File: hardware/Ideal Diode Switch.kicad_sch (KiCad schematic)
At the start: 0 parts

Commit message: Schematic is now mostly complete. Will review and then move onto the PCB layout
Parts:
- added C66, C67, C68, C69: 100nF/25VW, Capacitor_SMD:C_0603_1608Metric, symbol Device:C
- added J9: Conn_01x12, Connector_Phoenix_MSTB:PhoenixContact_MSTBVA_2,5_12-G-5,08_1x12_P5.08mm_Vertical, symbol Connector_Generic:Conn_01x12
- added Q10, Q11, Q12, Q5, Q6, Q7, Q8, Q9: SIR880BDP, BidirectionalSupply:POWERPAK-SO-8_L6.2-W5.2-P1.27-BL-EP, symbol BidirectionalSupply:SIR880BDP
- added R35, R39, R43, R47: 97.6K/0.1%, Resistor_SMD:R_0603_1608Metric, symbol Device:R
- added R36, R40, R44: 3.1K/0.1%, Resistor_SMD:R_0603_1608Metric, symbol Device:R
- added R37, R41, R45, R49: 2.1K/1%, Resistor_SMD:R_0603_1608Metric, symbol Device:R
- added R38, R42, R46, R50: 10K, Resistor_SMD:R_0603_1608Metric, symbol Device:R
- added R48: 3.1K/1%, Resistor_SMD:R_0603_1608Metric, symbol Device:R
- added U2, U6, U7, U8: LM74810QDRRRQ1, BidirectionalSupply:WSON-12_L3.0-W3.0-P0.50-TL-EP-2, symbol BidirectionalSupply:LM74810QDRRRQ1
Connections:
- new net: J9.6 (Pin_6), Q8.1 (S), Q8.2 (S), Q8.3 (S), U6.9 (OUT)
- new net: Q8.4 (G), U6.8 (HGATE)
- new net: C67.1, Q7.5 (D), Q7.6 (D), Q7.7 (D), Q7.8 (D), Q7.9 (EP), Q8.5 (D), Q8.6 (D), Q8.7 (D), Q8.8 (D), Q8.9 (EP), U6.10 (VS), U6.12 (C)
- new net: R40.2, R41.1, U6.5 (OV)
- new net: C67.2, U6.11 (CAP)
- new net: Q7.4 (G), U6.1 (DGATE)
- new net: R39.1, U6.4 (SW)
- new net: R36.2, R37.1, U2.5 (OV)
- new net: J9.12 (Pin_12), Q10.1 (S), Q10.2 (S), Q10.3 (S), U7.9 (OUT)
- new net: J9.3 (Pin_3), Q6.1 (S), Q6.2 (S), Q6.3 (S), U2.9 (OUT)
- new net: J9.9 (Pin_9), Q12.1 (S), Q12.2 (S), Q12.3 (S), U8.9 (OUT)
- new net: R47.1, U8.4 (SW)
- new net: C66.1, Q5.5 (D), Q5.6 (D), Q5.7 (D), Q5.8 (D), Q5.9 (EP), Q6.5 (D), Q6.6 (D), Q6.7 (D), Q6.8 (D), Q6.9 (EP), U2.10 (VS), U2.12 (C)
- new net: C66.2, U2.11 (CAP)
- new net: Q9.4 (G), U7.1 (DGATE)
- new net: C68.1, Q10.5 (D), Q10.6 (D), Q10.7 (D), Q10.8 (D), Q10.9 (EP), Q9.5 (D), Q9.6 (D), Q9.7 (D), Q9.8 (D), Q9.9 (EP), U7.10 (VS), U7.12 (C)
- new net: C68.2, U7.11 (CAP)
- new net: R43.1, U7.4 (SW)
- new net: R44.2, R45.1, U7.5 (OV)
- new net: Q10.4 (G), U7.8 (HGATE)
- new net: C69.1, Q11.5 (D), Q11.6 (D), Q11.7 (D), Q11.8 (D), Q11.9 (EP), Q12.5 (D), Q12.6 (D), Q12.7 (D), Q12.8 (D), Q12.9 (EP), U8.10 (VS), U8.12 (C)
- new net: C69.2, U8.11 (CAP)
- new net: Q5.4 (G), U2.1 (DGATE)
- new net: R35.1, U2.4 (SW)
- new net: Q6.4 (G), U2.8 (HGATE)
- new net: Q12.4 (G), U8.8 (HGATE)
- new net: R48.2, R49.1, U8.5 (OV)
- new net: Q11.4 (G), U8.1 (DGATE)
- new net GND: J9.1 (Pin_1), J9.10 (Pin_10), J9.4 (Pin_4), J9.7 (Pin_7), R37.2, R38.2, R41.2, R42.2, R45.2, R46.2, R49.2, R50.2, U2.7 (GND), U6.7 (GND), U7.7 (GND), U8.7 (GND)
- new net SW0_EN: R38.1, U2.6 (EN/UVLO)
- new net SW0_PWR: J9.2 (Pin_2), Q5.1 (S), Q5.2 (S), Q5.3 (S), U2.2 (A), U2.3 (VSNS)
- new net SW0_VSENSE: R35.2, R36.1
- new net SW1_EN: R42.1, U6.6 (EN/UVLO)
- new net SW1_PWR: J9.5 (Pin_5), Q7.1 (S), Q7.2 (S), Q7.3 (S), U6.2 (A), U6.3 (VSNS)
- new net SW1_VSENSE: R39.2, R40.1
- new net SW2_EN: R50.1, U8.6 (EN/UVLO)
- new net SW2_PWR: J9.8 (Pin_8), Q11.1 (S), Q11.2 (S), Q11.3 (S), U8.2 (A), U8.3 (VSNS)
- new net SW2_VSENSE: R47.2, R48.1
- new net SW3_EN: R46.1, U7.6 (EN/UVLO)
- new net SW3_PWR: J9.11 (Pin_11), Q9.1 (S), Q9.2 (S), Q9.3 (S), U7.2 (A), U7.3 (VSNS)
- new net SW3_VSENSE: R43.2, R44.1

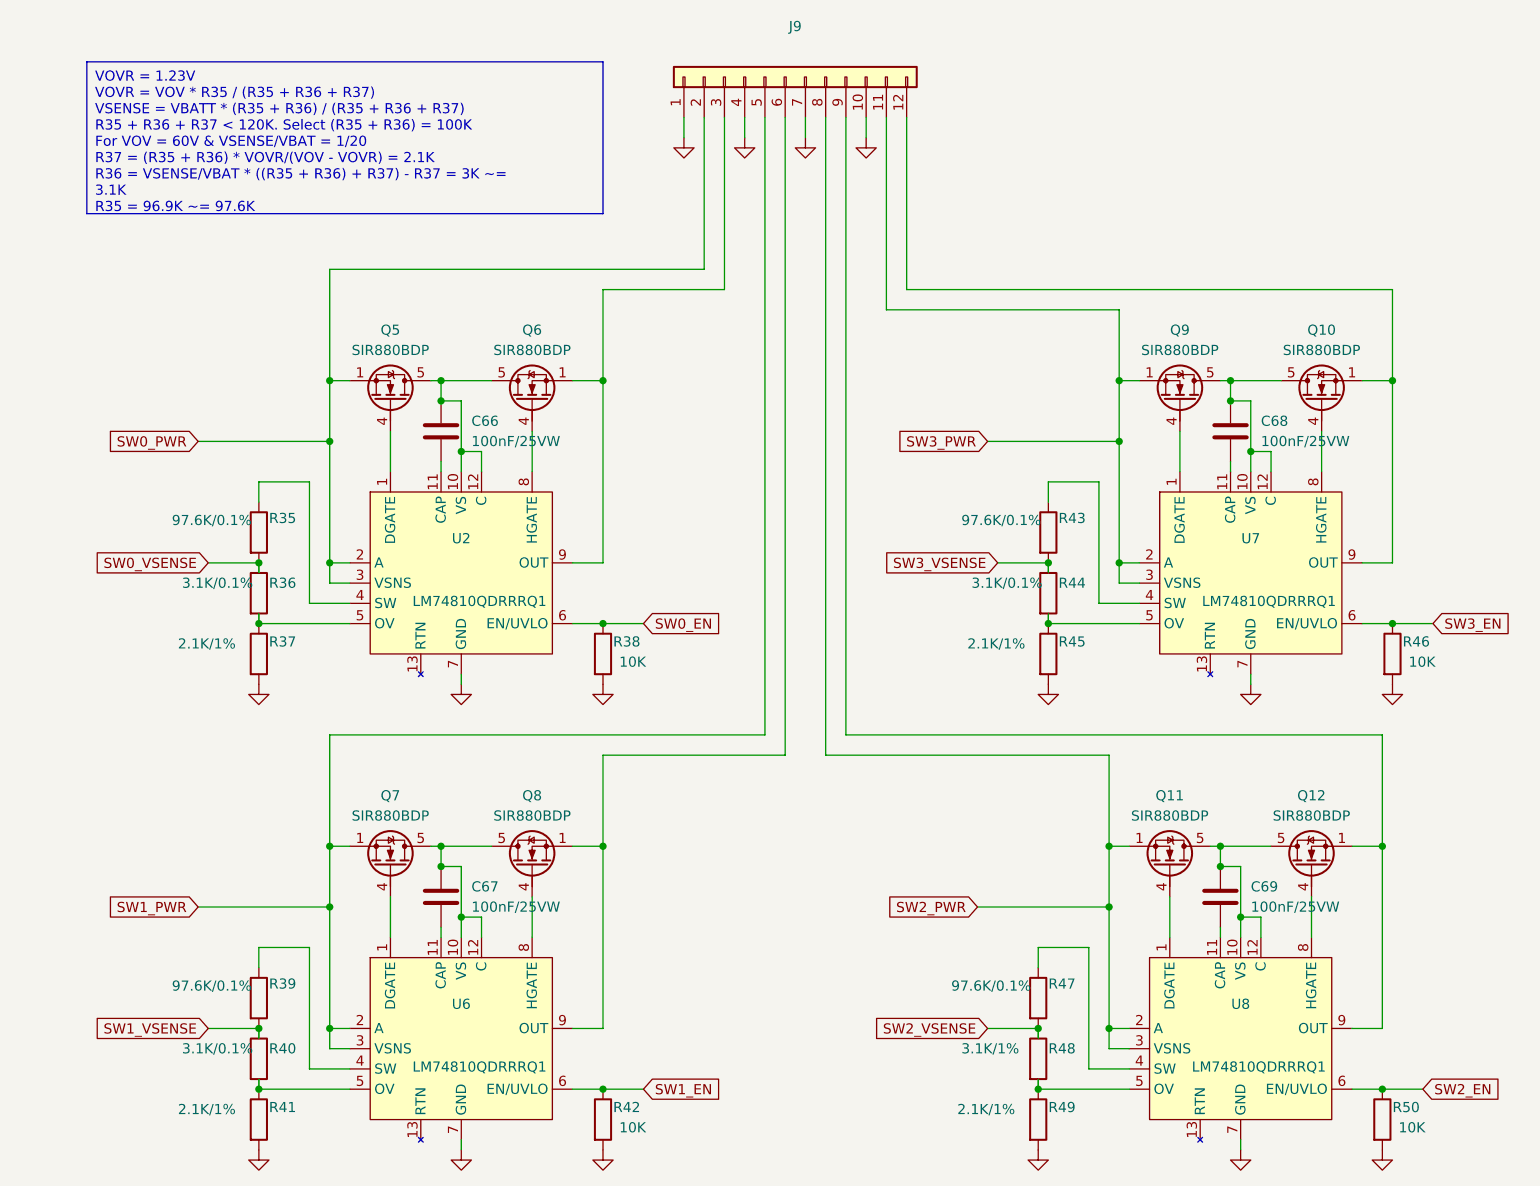
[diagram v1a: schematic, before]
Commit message: Checked all DC/DC converter capacitors Some part substitution to preference in stock items
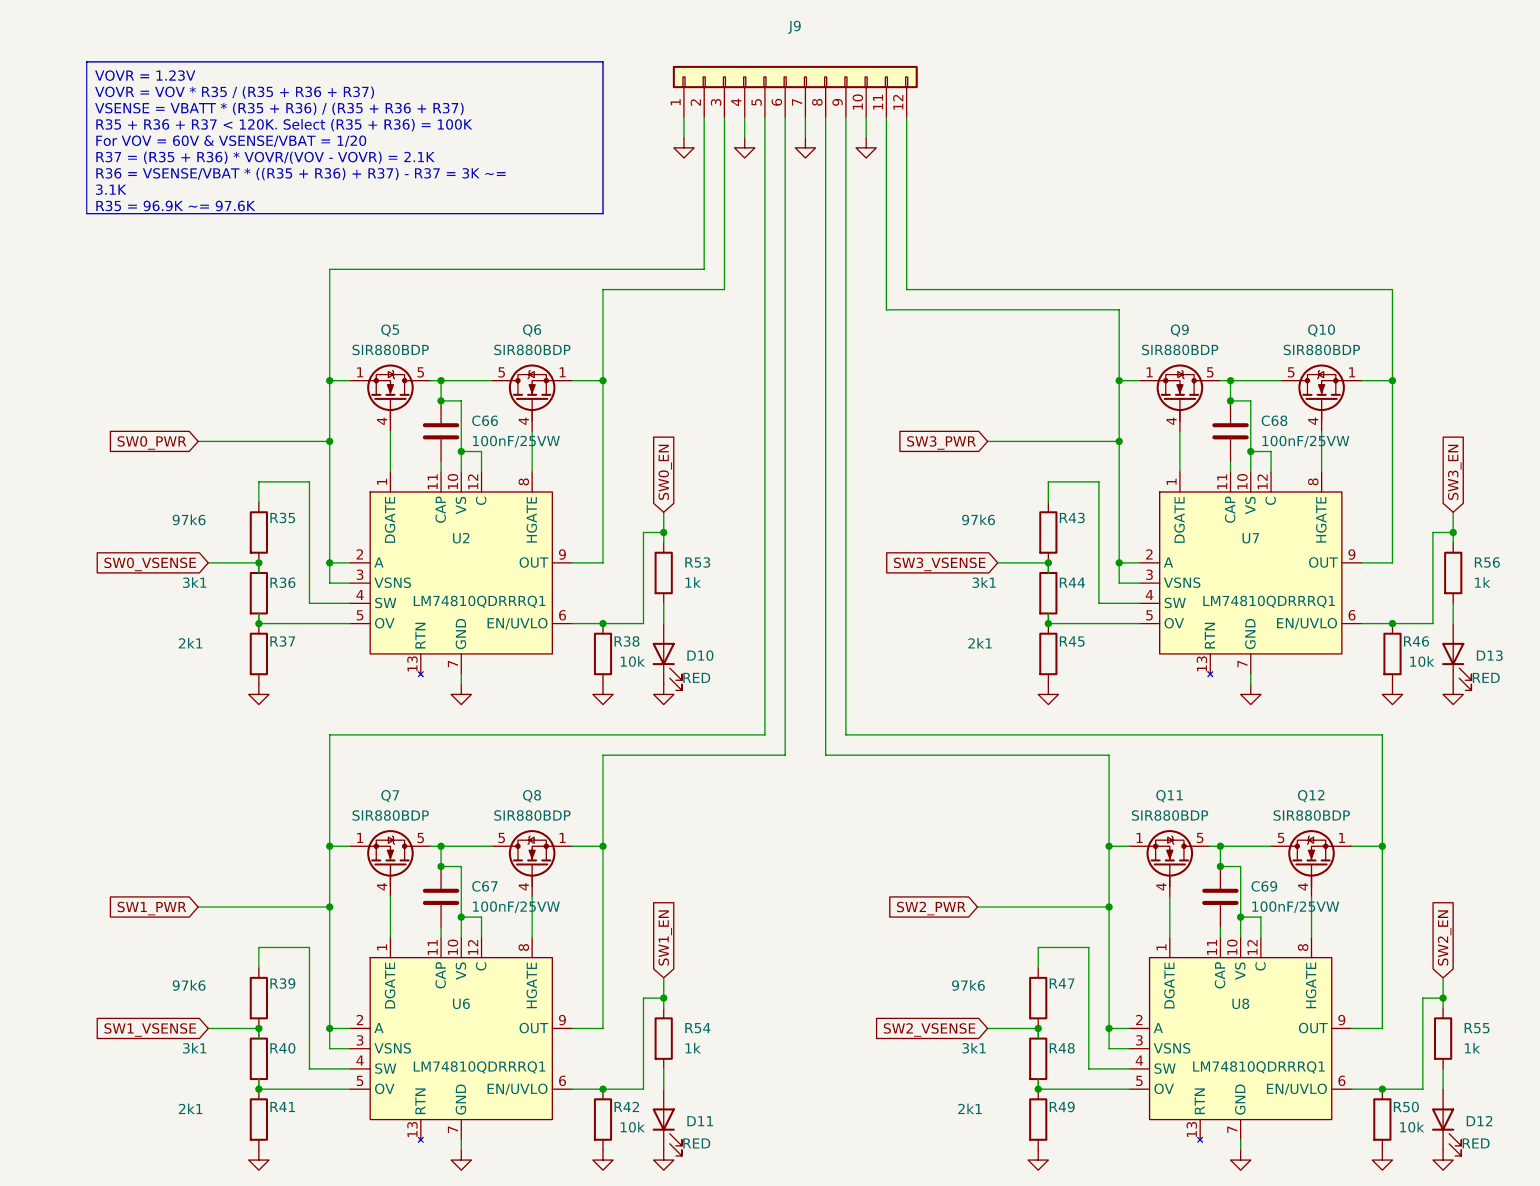
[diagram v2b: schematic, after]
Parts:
- added D10, D11, D12, D13: RED, LED_SMD:LED_0603_1608Metric, symbol Device:LED
- added R53, R54, R55, R56: 1k, Resistor_SMD:R_0603_1608Metric, symbol Device:R
- J9: Mouser (none) -> 651-1755833
- R35, R39, R43, R47: value 97.6K/0.1% -> 97k6; JLCPCB C861608 -> C2907079
- R36, R40, R44: value 3.1K/0.1% -> 3k1
- R37, R41, R45, R49: value 2.1K/1% -> 2k1; JLCPCB C861293 -> C22902
- R38, R42, R46, R50: value 10K -> 10k
- R48: value 3.1K/1% -> 3k1
- U2: JLCPCB C25804 -> C3215601
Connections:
- net GND: now also D10.1 (K), D11.1 (K), D12.1 (K), D13.1 (K)
- net SW0_EN: now also R53.1
- net SW1_EN: now also R54.1
- net SW2_EN: now also R55.1
- net SW3_EN: now also R56.1
- new net: D11.2 (A), R54.2
- new net: D13.2 (A), R56.2
- new net: D10.2 (A), R53.2
- new net: D12.2 (A), R55.2

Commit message: All components placed on board and most 3D shapes are present
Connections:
- net SW0_PWR: no longer names the net of J9.2 (Pin_2), Q5.1 (S), Q5.2 (S), Q5.3 (S), U2.2 (A), U2.3 (VSNS)
- net SW1_PWR: no longer names the net of J9.5 (Pin_5), Q7.1 (S), Q7.2 (S), Q7.3 (S), U6.2 (A), U6.3 (VSNS)
- net SW2_PWR: no longer names the net of J9.8 (Pin_8), Q11.1 (S), Q11.2 (S), Q11.3 (S), U8.2 (A), U8.3 (VSNS)
- net SW3_PWR: no longer names the net of J9.11 (Pin_11), Q9.1 (S), Q9.2 (S), Q9.3 (S), U7.2 (A), U7.3 (VSNS)
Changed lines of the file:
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@@
-	)
-	(junction
-		(at 152.4 68.58)
-		(diameter 0)
-		(color 0 0 0 0)
 	)
 	(junction
@@
 	)
 	(junction
-		(at 53.34 68.58)
-		(diameter 0)
-		(color 0 0 0 0)
-	)
-	(junction
 		(at 185.42 119.38)
-		(diameter 0)
-		(color 0 0 0 0)
-	)
-	(junction
-		(at 151.13 127)
 		(diameter 0)
 		(color 0 0 0 0)
@@
 	)
 	(junction
-		(at 53.34 127)
-		(diameter 0)
-		(color 0 0 0 0)
-	)
-	(junction
 		(at 53.34 83.82)
 		(diameter 0)
@@
 	(wire
 		(pts
-			(xy 151.13 119.38) (xy 151.13 127)
+			(xy 151.13 119.38) (xy 151.13 142.24)
 		)
 		(stroke
@@
 	(wire
 		(pts
-			(xy 53.34 60.96) (xy 53.34 68.58)
+			(xy 53.34 60.96) (xy 53.34 83.82)
 		)
 		(stroke
@@
 	(wire
 		(pts
-			(xy 151.13 127) (xy 151.13 142.24)
-		)
-		(stroke
-			(width 0)
-			(type default)
-		)
-	)
-	(wire
-		(pts
 			(xy 87.63 149.86) (xy 92.71 149.86)
 		)
@@
 	(wire
 		(pts
-			(xy 134.62 127) (xy 151.13 127)
-		)
-		(stroke
-			(width 0)
-			(type default)
-		)
-	)
-	(wire
-		(pts
 			(xy 87.63 107.95) (xy 110.49 107.95)
 		)
@@
 	(wire
 		(pts
-			(xy 53.34 68.58) (xy 53.34 83.82)
-		)
-		(stroke
-			(width 0)
-			(type default)
-		)
-	)
-	(wire
-		(pts
 			(xy 176.53 125.73) (xy 176.53 130.81)
 		)
@@
 	(wire
 		(pts
-			(xy 53.34 119.38) (xy 53.34 127)
+			(xy 53.34 119.38) (xy 53.34 142.24)
 		)
 		(stroke
@@
 	(wire
 		(pts
-			(xy 152.4 68.58) (xy 152.4 83.82)
+			(xy 152.4 60.96) (xy 152.4 83.82)
 		)
 		(stroke
@@
 	(wire
 		(pts
-			(xy 36.83 68.58) (xy 53.34 68.58)
-		)
-		(stroke
-			(width 0)
-			(type default)
-		)
-	)
-	(wire
-		(pts
 			(xy 165.1 121.92) (xy 167.64 121.92)
 		)
@@
 	(wire
 		(pts
-			(xy 135.89 68.58) (xy 152.4 68.58)
-		)
-		(stroke
-			(width 0)
-			(type default)
-		)
-	)
-	(wire
-		(pts
 			(xy 100.33 27.94) (xy 100.33 46.99)
 		)
@@
 	(wire
 		(pts
-			(xy 36.83 127) (xy 53.34 127)
-		)
-		(stroke
-			(width 0)
-			(type default)
-		)
-	)
-	(wire
-		(pts
 			(xy 83.82 119.38) (xy 87.63 119.38)
 		)
@@
 	(wire
 		(pts
-			(xy 152.4 60.96) (xy 152.4 68.58)
-		)
-		(stroke
-			(width 0)
-			(type default)
-		)
-	)
-	(wire
-		(pts
 			(xy 53.34 60.96) (xy 55.88 60.96)
 		)
@@
 		(pts
 			(xy 66.04 119.38) (xy 67.31 119.38)
-		)
-		(stroke
-			(width 0)
-			(type default)
-		)
-	)
-	(wire
-		(pts
-			(xy 53.34 127) (xy 53.34 142.24)
 		)
 		(stroke
@@
 			)
 			(justify left top)
-		)
-	)
-	(global_label "SW3_PWR"
-		(shape input)
-		(at 135.89 68.58 180)
-		(fields_autoplaced yes)
-		(effects
-			(font
-				(size 1.27 1.27)
-			)
-			(justify right)
-		)
-		(property "Intersheetrefs" "${INTERSHEET_REFS}"
-			(at 124.0754 68.58 0)
-			(effects
-				(font
-					(size 1.27 1.27)
-				)
-				(justify right)
-				(hide yes)
-			)
 		)
 	)
@@
 		)
 	)
-	(global_label "SW0_PWR"
-		(shape input)
-		(at 36.83 68.58 180)
-		(fields_autoplaced yes)
-		(effects
-			(font
-				(size 1.27 1.27)
-			)
-			(justify right)
-		)
-		(property "Intersheetrefs" "${INTERSHEET_REFS}"
-			(at 25.0154 68.58 0)
-			(effects
-				(font
-					(size 1.27 1.27)
-				)
-				(justify right)
-				(hide yes)
-			)
-		)
-	)
 	(global_label "SW0_EN"
 		(shape input)
@@
 		)
 	)
-	(global_label "SW2_PWR"
-		(shape input)
-		(at 134.62 127 180)
-		(fields_autoplaced yes)
-		(effects
-			(font
-				(size 1.27 1.27)
-			)
-			(justify right)
-		)
-		(property "Intersheetrefs" "${INTERSHEET_REFS}"
-			(at 122.8054 127 0)
-			(effects
-				(font
-					(size 1.27 1.27)
-				)
-				(justify right)
-				(hide yes)
-			)
-		)
-	)
 	(global_label "SW0_VSENSE"
 		(shape input)
@@
 				(hide yes)
 			)
-		)
-	)
-	(global_label "SW1_PWR"
-		(shape input)
-		(at 36.83 127 180)
-		(fields_autoplaced yes)
-		(effects
-			(font
-				(size 1.27 1.27)
-			)
-			(justify right)
-		)
-		(property "Intersheetrefs" "${INTERSHEET_REFS}"
-			(at 25.0154 127 0)
-			(effects
-				(font
-					(size 1.27 1.27)
-				)
-				(justify right)
-				(hide yes)
-			)
